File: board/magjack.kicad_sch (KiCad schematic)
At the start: 1 part, among them J2 LPJ4265BDNL

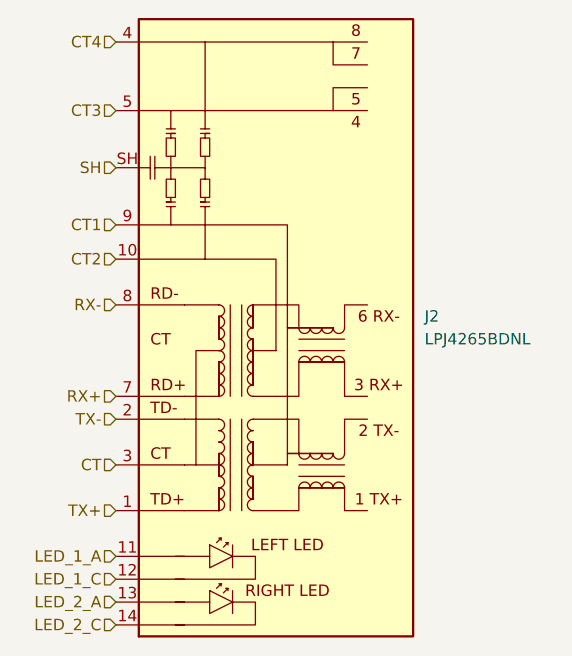
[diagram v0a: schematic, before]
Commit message: added LDO
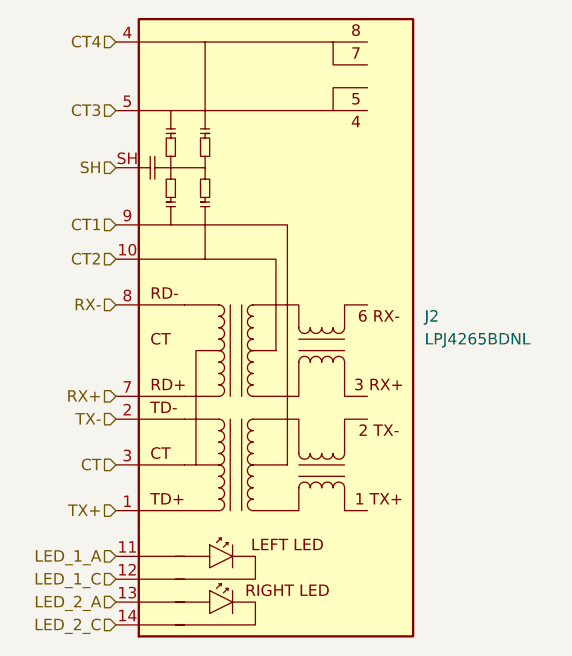
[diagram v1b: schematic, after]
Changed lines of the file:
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@@
-(kicad_sch (version 20211123) (generator eeschema)
+(kicad_sch (version 20230121) (generator eeschema)
   (paper "A4")
-  (hierarchical_label "CT2" (shape input) (at 143.51 97.79 180)
+  (hierarchical_label "CT2" (shape input) (at 143.51 97.79 180) (fields_autoplaced)
     (effects (font (size 1.27 1.27)) (justify right))
   )
-  (hierarchical_label "CT1" (shape input) (at 143.51 93.98 180)
+  (hierarchical_label "CT1" (shape input) (at 143.51 93.98 180) (fields_autoplaced)
     (effects (font (size 1.27 1.27)) (justify right))
   )
-  (hierarchical_label "CT4" (shape input) (at 143.51 73.66 180)
+  (hierarchical_label "CT4" (shape input) (at 143.51 73.66 180) (fields_autoplaced)
     (effects (font (size 1.27 1.27)) (justify right))
   )
-  (hierarchical_label "LED_1_C" (shape input) (at 143.51 133.35 180)
+  (hierarchical_label "LED_1_C" (shape input) (at 143.51 133.35 180) (fields_autoplaced)
     (effects (font (size 1.27 1.27)) (justify right))
   )
-  (hierarchical_label "TX+" (shape input) (at 143.51 125.73 180)
+  (hierarchical_label "TX+" (shape input) (at 143.51 125.73 180) (fields_autoplaced)
     (effects (font (size 1.27 1.27)) (justify right))
   )
-  (hierarchical_label "LED_2_C" (shape input) (at 143.51 138.43 180)
+  (hierarchical_label "LED_2_C" (shape input) (at 143.51 138.43 180) (fields_autoplaced)
     (effects (font (size 1.27 1.27)) (justify right))
   )
-  (hierarchical_label "LED_2_A" (shape input) (at 143.51 135.89 180)
+  (hierarchical_label "LED_2_A" (shape input) (at 143.51 135.89 180) (fields_autoplaced)
     (effects (font (size 1.27 1.27)) (justify right))
   )
-  (hierarchical_label "RX-" (shape input) (at 143.51 102.87 180)
+  (hierarchical_label "RX-" (shape input) (at 143.51 102.87 180) (fields_autoplaced)
     (effects (font (size 1.27 1.27)) (justify right))
   )
-  (hierarchical_label "CT3" (shape input) (at 143.51 81.28 180)
+  (hierarchical_label "CT3" (shape input) (at 143.51 81.28 180) (fields_autoplaced)
     (effects (font (size 1.27 1.27)) (justify right))
   )
-  (hierarchical_label "LED_1_A" (shape input) (at 143.51 130.81 180)
+  (hierarchical_label "LED_1_A" (shape input) (at 143.51 130.81 180) (fields_autoplaced)
     (effects (font (size 1.27 1.27)) (justify right))
   )
-  (hierarchical_label "TX-" (shape input) (at 143.51 115.57 180)
+  (hierarchical_label "TX-" (shape input) (at 143.51 115.57 180) (fields_autoplaced)
     (effects (font (size 1.27 1.27)) (justify right))
   )
-  (hierarchical_label "SH" (shape input) (at 143.51 87.63 180)
+  (hierarchical_label "SH" (shape input) (at 143.51 87.63 180) (fields_autoplaced)
     (effects (font (size 1.27 1.27)) (justify right))
   )
-  (hierarchical_label "CT" (shape input) (at 143.51 120.65 180)
+  (hierarchical_label "CT" (shape input) (at 143.51 120.65 180) (fields_autoplaced)
     (effects (font (size 1.27 1.27)) (justify right))
   )
-  (hierarchical_label "RX+" (shape input) (at 143.51 113.03 180)
+  (hierarchical_label "RX+" (shape input) (at 143.51 113.03 180) (fields_autoplaced)
     (effects (font (size 1.27 1.27)) (justify right))
   )
   (symbol (lib_id "b135:LPJ4265BDNL") (at 161.29 105.41 0) (unit 1)
-    (in_bom yes) (on_board yes) (fields_autoplaced)
-    (property "Reference" "J2" (id 0) (at 177.8 104.1399 0)
+    (in_bom yes) (on_board yes) (dnp no) (fields_autoplaced)
+    (property "Reference" "J2" (at 177.8 104.1399 0)
       (effects (font (size 1.27 1.27)) (justify left))
     )
-    (property "Value" "LPJ4265BDNL" (id 1) (at 177.8 106.6799 0)
+    (property "Value" "LPJ4265BDNL" (at 177.8 106.6799 0)
       (effects (font (size 1.27 1.27)) (justify left))
     )
-    (property "Footprint" "b135:LPJ4265BDNL" (id 2) (at 161.29 69.85 0)
+    (property "Footprint" "b135:LPJ4265BDNL" (at 161.29 69.85 0)
       (effects (font (size 1.27 1.27)) hide)
     )
-    (property "Datasheet" "https://www.l-p.com/file/datasheet/lpj4265bdnl.pdf" (id 3) (at 157.48 127 0)
+    (property "Datasheet" "https://www.l-p.com/file/datasheet/lpj4265bdnl.pdf" (at 157.48 127 0)
       (effects (font (size 1.27 1.27)) hide)
     )
-    (property "MPN" "LPJ4265BDNL" (id 4) (at 161.29 105.41 0)
+    (property "MPN" "LPJ4265BDNL" (at 161.29 105.41 0)
       (effects (font (size 1.27 1.27)) hide)
     )
@@
     (pin "9")
     (pin "SH")
+    (instances
+      (project "board"
+        (path "/57732dd3-1162-4c3f-88bd-31bf473d124d/c5ffe30d-7e51-4dad-b268-ea446309615a"
+          (reference "J2") (unit 1)
+        )
+      )
+    )
   )
 )
